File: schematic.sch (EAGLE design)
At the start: 82 parts, among them X1 SSW-108-02-S-D-RA, X2 SSW-116-02-S-TRA, X3 SSW-106-02-S-D-RA, X4 SSW-116-02-S-TRA

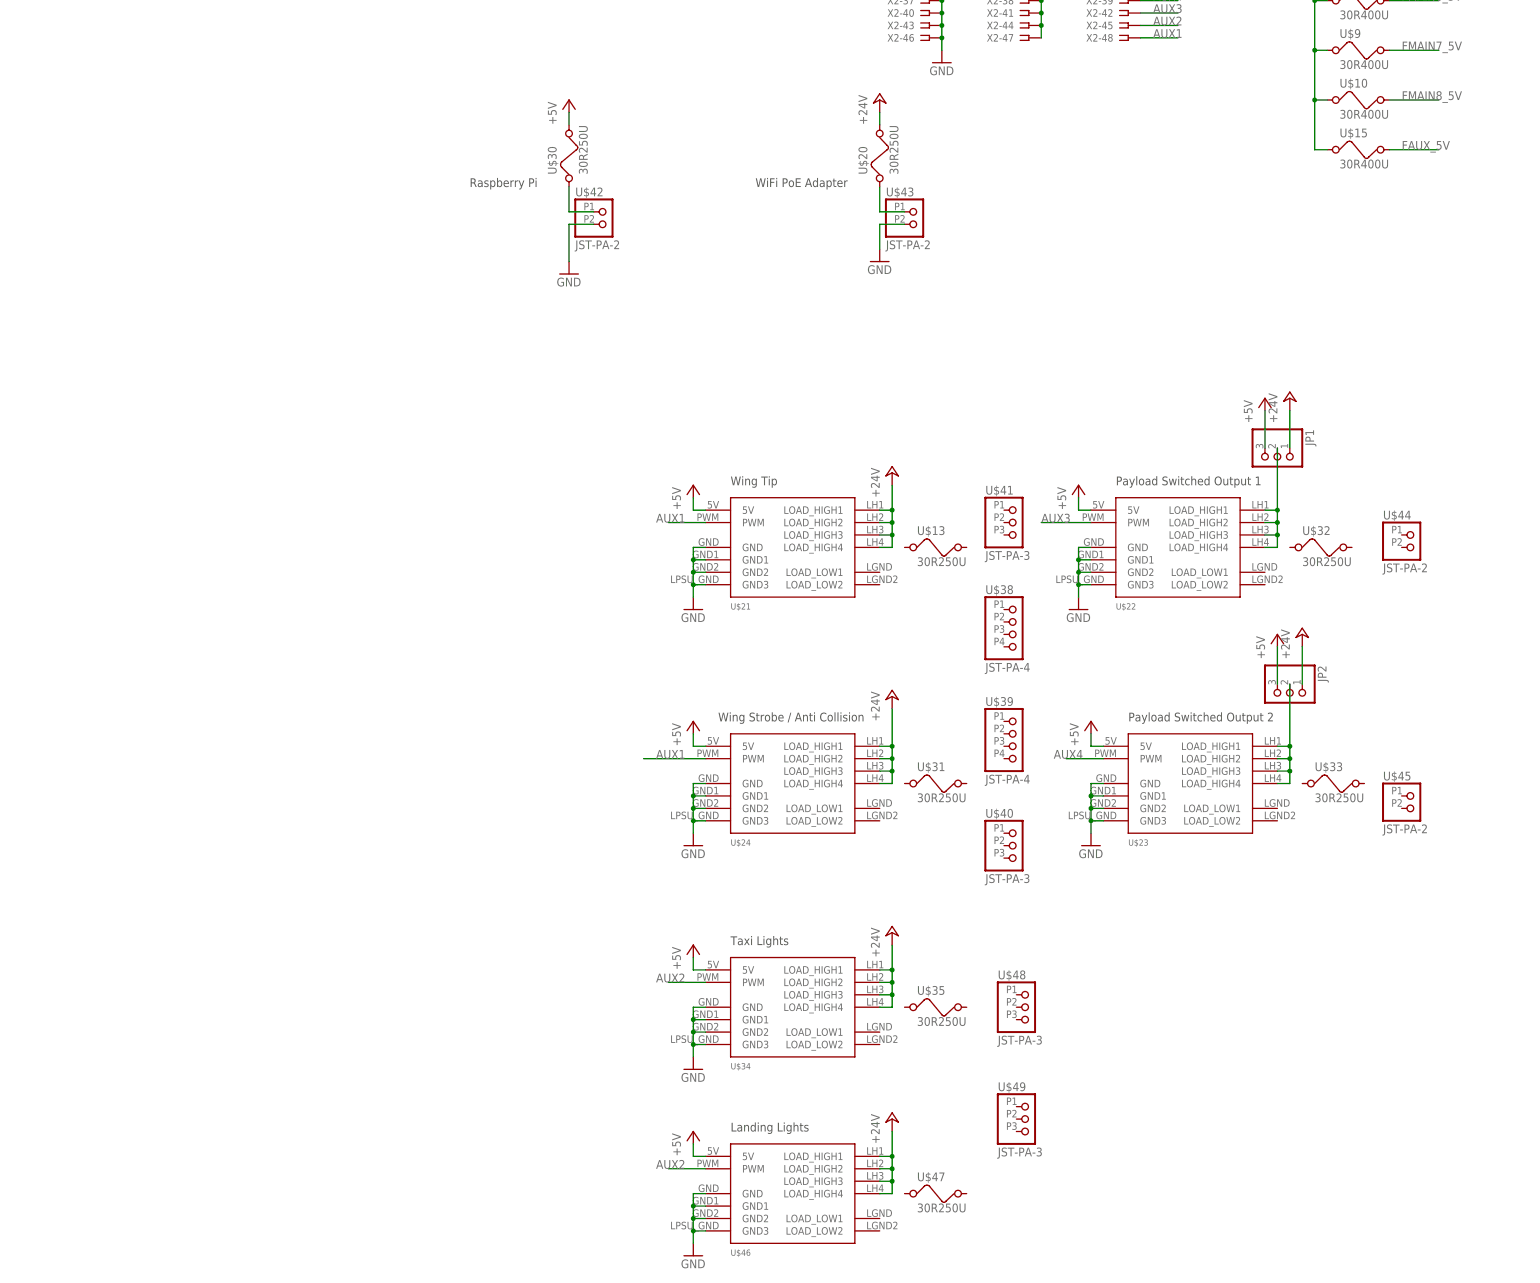
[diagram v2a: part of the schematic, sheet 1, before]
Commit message: Adding 12v rail and connecting payloads.
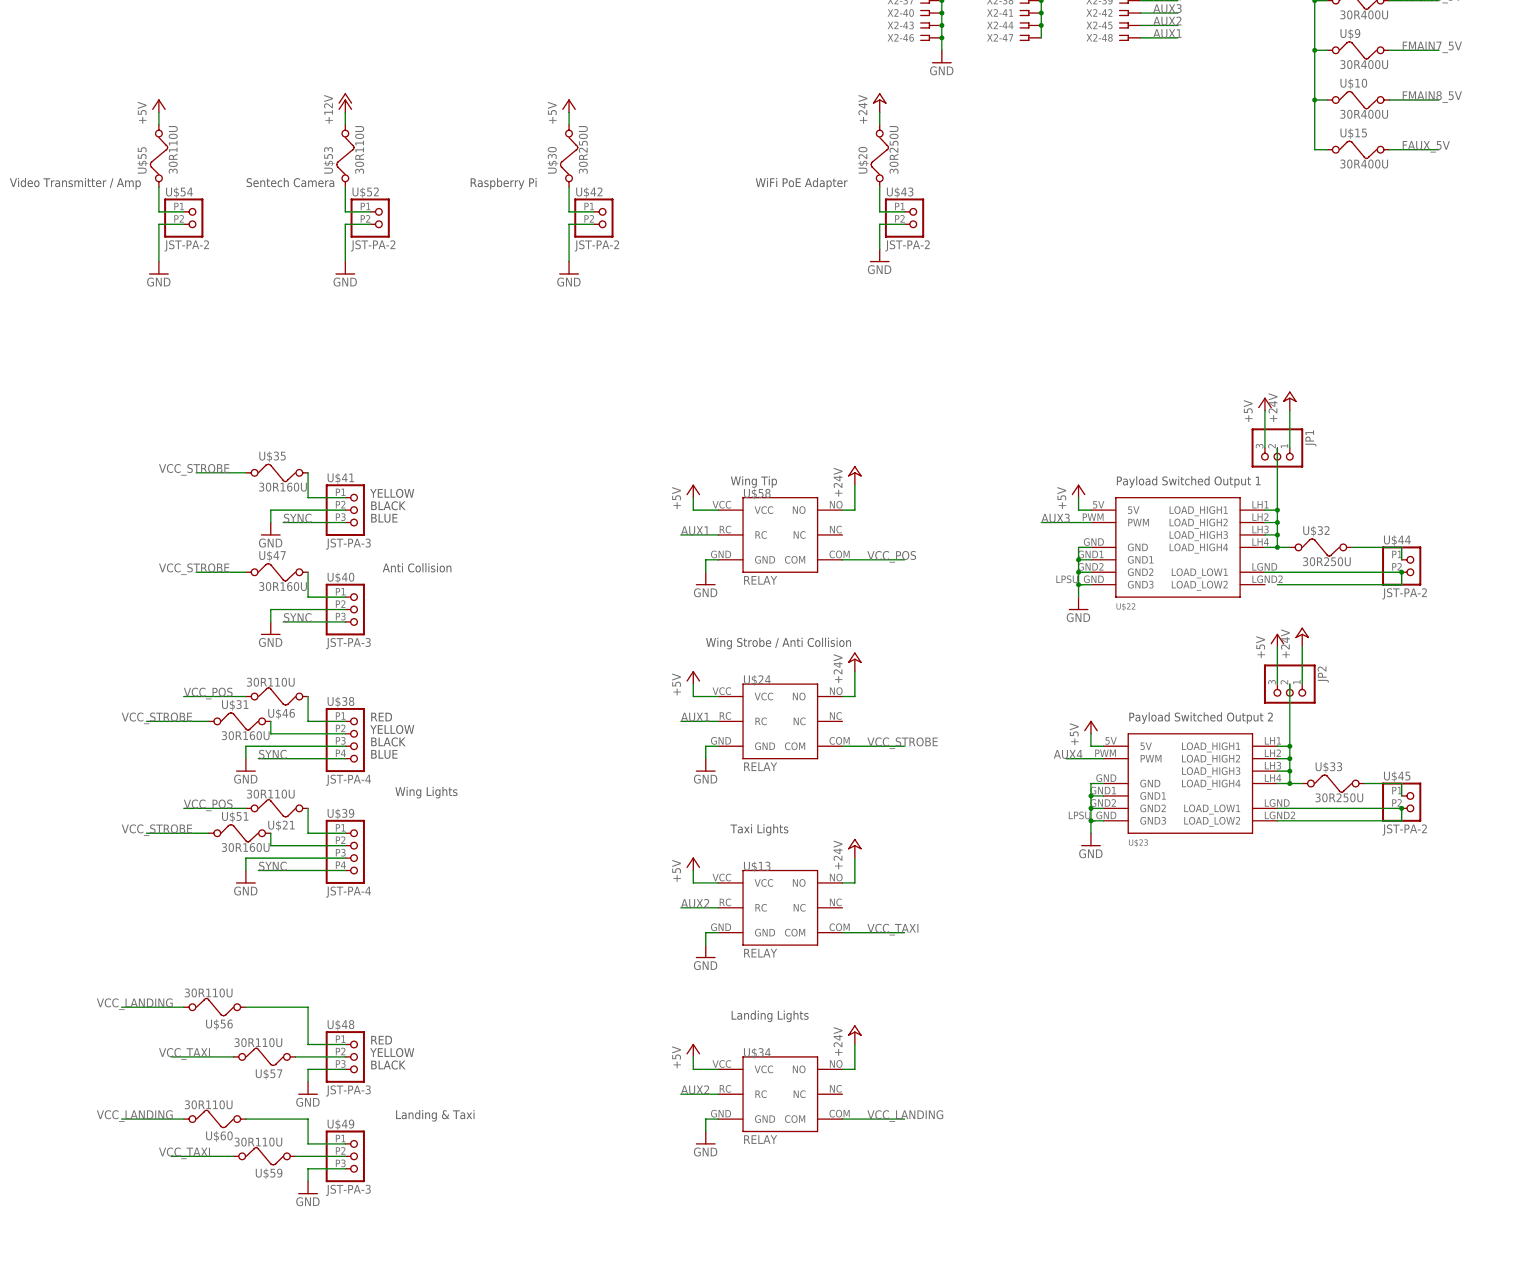
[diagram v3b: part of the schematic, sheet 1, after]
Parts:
- added C10, C9: (no value), rcl:C-USC1210
- added LED3: (no value), led:LEDCHIPLED_0805
- added R16: (no value), rcl:R-US_M0805
- added U$50: PYB10, cui:PYB10
- added U$51: 30R160U, littelfuse:30R160U
- added U$52, U$54: JST-PA-2, jst:JST-PA-2
- added U$53, U$55, U$56, U$57, U$59, U$60: 30R110U, littelfuse:30R110U
- added U$58: RELAY, pololu:RELAY
- U$13: value 30R250U -> RELAY; device littelfuse:30R250U -> pololu:RELAY
- U$2: value VHE100W -> VHB150W; device cui:VHE100W -> cui:VHB150W
- U$21, U$46: value MED_MOSFET -> 30R110U; device pololu:MED_MOSFET -> littelfuse:30R110U
- U$24, U$34: value MED_MOSFET -> RELAY; device pololu:MED_MOSFET -> pololu:RELAY
- U$31, U$35, U$47: value 30R250U -> 30R160U; device littelfuse:30R250U -> littelfuse:30R160U
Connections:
- new net +12V: LED3.A, U$50.VO+, U$53.2
- new net 12V_ONOFF: U$29.1A1, U$50.CTRL
- new net N$14: U$52.1, U$53.1
- new net N$20: U$54.1, U$55.1
- new net N$21: LED3.C, R16.2
- new net N$22: U$23.LOAD_LOW1, U$23.LOAD_LOW2, U$45.2
- new net N$23: U$33.2, U$45.1
- new net N$24: U$22.LOAD_LOW1, U$44.2
- new net N$25: U$32.2, U$44.1
- new net N$26: U$38.1, U$46.1
- new net N$27: U$31.2, U$38.2
- new net N$28: U$21.1, U$39.1
- new net N$29: U$39.2, U$51.2
- new net N$30: U$35.2, U$41.1
- new net N$31: U$40.1, U$47.2
- new net N$32: U$49.2, U$59.1
- new net N$33: U$49.1, U$60.1
- new net N$34: U$48.2, U$57.1
- new net N$35: U$48.1, U$56.1
- new net SYNC: U$38.4, U$39.4, U$40.3, U$41.3
- new net VCC_LANDING: U$34.COM, U$56.2, U$60.2
- new net VCC_POS: U$21.2, U$46.2, U$58.COM
- new net VCC_STROBE: U$24.COM, U$31.1, U$35.1, U$47.1, U$51.1
- new net VCC_TAXI: U$13.COM, U$57.2, U$59.2
- net +24V: now also U$13.NO, U$24.NO, U$34.NO, U$58.NO; no longer U$21.LOAD_HIGH1, U$21.LOAD_HIGH2, U$21.LOAD_HIGH3, U$21.LOAD_HIGH4, U$24.LOAD_HIGH1, U$24.LOAD_HIGH2, U$24.LOAD_HIGH3, U$24.LOAD_HIGH4, U$34.LOAD_HIGH1, U$34.LOAD_HIGH2, U$34.LOAD_HIGH3, U$34.LOAD_HIGH4, U$46.LOAD_HIGH1, U$46.LOAD_HIGH2, U$46.LOAD_HIGH3, U$46.LOAD_HIGH4
- net +5V: now also U$13.VCC, U$24.VCC, U$34.VCC, U$55.2, U$58.VCC; no longer U$21.5V, U$24.5V, U$34.5V, U$46.5V
- net 24V_ONOFF: no longer U$29.1A1
- net AUX1: now also U$24.RC, U$58.RC; no longer U$21.PWM, U$24.PWM
- net AUX2: now also U$13.RC, U$34.RC; no longer U$34.PWM, U$46.PWM
- net GND: now also R16.1, U$13.GND, U$38.3, U$39.3, U$40.2, U$41.2, U$48.3, U$49.3, U$50.VO-, U$52.2, U$54.2, U$58.GND; no longer U$21.GND, U$21.GND1, U$21.GND2, U$21.GND3, U$24.GND1, U$24.GND2, U$24.GND3, U$34.GND1, U$34.GND2, U$34.GND3, U$46.GND, U$46.GND1, U$46.GND2, U$46.GND3
- net N$16: now also U$33.1
- net N$4: now also U$32.1
- net V+: now also C10.1, C9.1, U$50.VIN; no longer U$28.NC, U$28.NC1, U$29.NC, U$29.NC1
- net V-: now also C10.2, C9.2, U$50.GND
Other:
- note added: "Anti Collision"
- note added: "BLACK"
- note added: "BLUE"
- note added: "Landing & Taxi"
- note added: "RED"
- note added: "Sentech Camera"
- note added: "Video Transmitter / Amp"
- note added: "Wing Lights"
- note added: "YELLOW"
- moved on the sheet: U$31, U$35, U$38, U$39, U$40, U$41, U$44, U$47, U$48, U$49

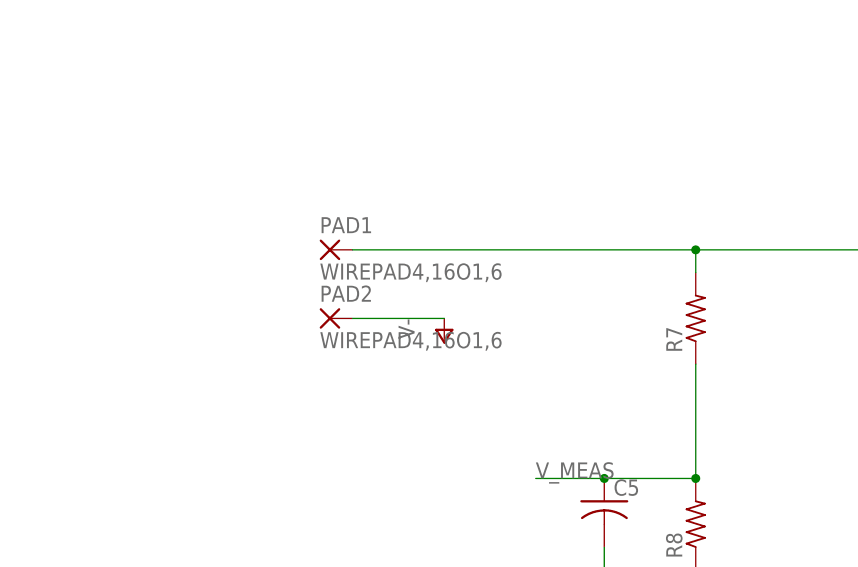
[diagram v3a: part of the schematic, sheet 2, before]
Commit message: Adding new power connector.
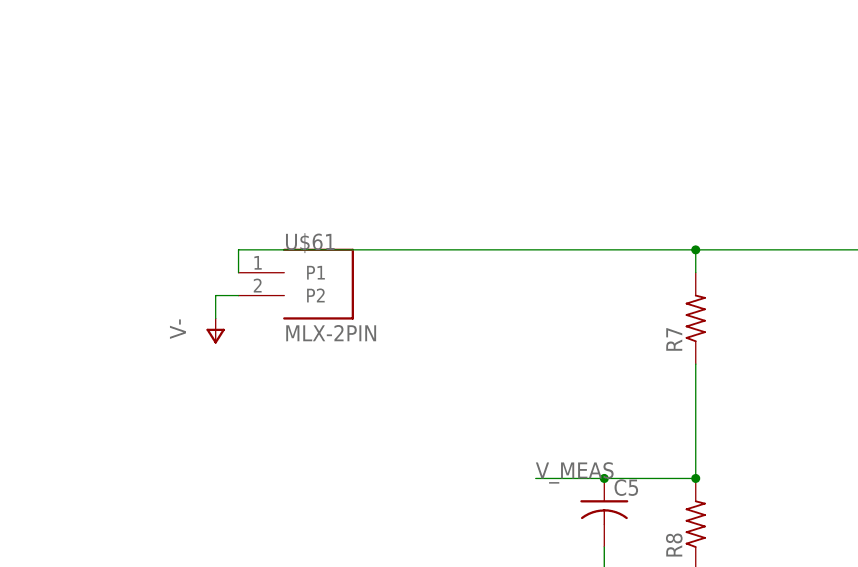
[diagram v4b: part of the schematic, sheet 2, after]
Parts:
- removed PAD1, PAD2: WIREPAD4,16O1,6, wirepad:WIREPAD4,16O1,6
- added U$61: MLX-2PIN, molex:MLX-2PIN
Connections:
- net N$12: now also U$61.P1; no longer PAD1.P
- net V-: now also U$61.P2; no longer PAD2.P
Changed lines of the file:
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@@
 <part name="X2" library="con-samtec" deviceset="SSW-116-02-S-T" device="RA"/>
 <part name="X3" library="con-samtec" deviceset="SSW-106-02-S-D" device="-RA"/>
-<part name="PAD1" library="wirepad" deviceset="WIREPAD" device="4,16O1,6"/>
-<part name="PAD2" library="wirepad" deviceset="WIREPAD" device="4,16O1,6"/>
 <part name="U$1" library="cui" deviceset="VHE100W" device=""/>
 <part name="U$3" library="littelfuse" deviceset="30R400U" device=""/>
@@
 <part name="U$21" library="littelfuse" deviceset="30R110U" device=""/>
 <part name="U$46" library="littelfuse" deviceset="30R110U" device=""/>
+<part name="U$61" library="molex" deviceset="MLX-2PIN" device=""/>
 </parts>
 <sheets>
@@
 </plain>
 <instances>
-<instance part="PAD1" gate="G$1" x="170.18" y="83.82"/>
-<instance part="PAD2" gate="G$1" x="170.18" y="76.2"/>
 <instance part="U$1" gate="G$1" x="-43.18" y="106.68"/>
-<instance part="P-1" gate="1" x="182.88" y="73.66"/>
+<instance part="P-1" gate="1" x="157.48" y="73.66"/>
 <instance part="P+2" gate="1" x="-81.28" y="33.02"/>
 <instance part="P-2" gate="1" x="-81.28" y="99.06"/>
@@
 <instance part="P+35" gate="1" x="-25.4" y="-43.18"/>
 <instance part="GND33" gate="1" x="-25.4" y="-68.58"/>
+<instance part="U$61" gate="G$1" x="165.1" y="78.74"/>
 </instances>
 <busses>
@@
 <net name="V-" class="0">
 <segment>
-<pinref part="P-1" gate="1" pin="V-"/>
-<pinref part="PAD2" gate="G$1" pin="P"/>
-<wire x1="182.88" y1="76.2" x2="172.72" y2="76.2" width="0.1524" layer="91"/>
-</segment>
-<segment>
 <pinref part="C3" gate="G$1" pin="1"/>
 <pinref part="P-2" gate="1" pin="V-"/>
@@
 <junction x="-76.2" y="-63.5"/>
 </segment>
+<segment>
+<pinref part="U$61" gate="G$1" pin="P2"/>
+<pinref part="P-1" gate="1" pin="V-"/>
+<wire x1="160.02" y1="78.74" x2="157.48" y2="78.74" width="0.1524" layer="91"/>
+<wire x1="157.48" y1="78.74" x2="157.48" y2="76.2" width="0.1524" layer="91"/>
+</segment>
 </net>
 <net name="V+" class="0">
@@
 <wire x1="236.22" y1="83.82" x2="246.38" y2="83.82" width="0.1524" layer="91"/>
 <wire x1="210.82" y1="81.28" x2="210.82" y2="83.82" width="0.1524" layer="91"/>
-<junction x="210.82" y="83.82"/>
 <pinref part="U$17" gate="G$1" pin="VIN-"/>
 <wire x1="246.38" y1="81.28" x2="246.38" y2="83.82" width="0.1524" layer="91"/>
@@
 <wire x1="236.22" y1="66.04" x2="236.22" y2="83.82" width="0.1524" layer="91"/>
 <junction x="236.22" y="83.82"/>
-<pinref part="PAD1" gate="G$1" pin="P"/>
-<wire x1="172.72" y1="83.82" x2="210.82" y2="83.82" width="0.1524" layer="91"/>
-</segment>
-</net>
+<pinref part="U$61" gate="G$1" pin="P1"/>
+<wire x1="160.02" y1="81.28" x2="160.02" y2="83.82" width="0.1524" layer="91"/>
+<wire x1="160.02" y1="83.82" x2="210.82" y2="83.82" width="0.1524" layer="91"/>
+<junction x="210.82" y="83.82"/>
+</segment>
+</net>

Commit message: Removing some components space doesn't allow for.  Established basic layout.
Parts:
- removed C10, C9: (no value), rcl:C-USC1210
- removed JP2: (no value), pinhead:PINHD-1X3
- removed LED3: (no value), led:LEDCHIPLED_0805
- removed R16: (no value), rcl:R-US_M0805
- removed U$11: 30R160U, littelfuse:30R160U
- removed U$23: MED_MOSFET, pololu:MED_MOSFET
- removed U$33: 30R250U, littelfuse:30R250U
- removed U$34: RELAY, pololu:RELAY
- removed U$45, U$52: JST-PA-2, jst:JST-PA-2
- removed U$50: PYB10, cui:PYB10
- removed U$53: 30R110U, littelfuse:30R110U
- added F30: 30R160U, littelfuse:30R160U
- added H1, H2, H3, H4: MOUNT-HOLE3.6, holes:MOUNT-HOLE3.6
- added J2: MLX-2PIN, molex:MLX-2PIN
- renumbered U$1 to U1, U$10 to F8, U$12 to F29, U$13 to U9, U$14 to J5, U$15 to F9, U$16 to F10, U$17 to U6, U$18 to J3, U$19 to F28, U$2 to U2, U$20 to F11, U$21 to F22, U$22 to U11, U$24 to U8, U$25 to U4, U$26 to U5, U$27 to J4, U$28 to SW1, U$29 to SW2, U$3 to F1, U$30 to F12, U$31 to F21, U$32 to F16, U$35 to F18, U$36 to F15, U$37 to J10, U$38 to J19, U$39 to J20, U$4 to F2, U$40 to J18, U$41 to J17, U$42 to J12, U$43 to J11, U$44 to J15, U$46 to F20, U$47 to F19, U$48 to J21, U$49 to J22, U$5 to F3, U$51 to F23, U$54 to J14, U$55 to F14, U$56 to F24, U$57 to F25, U$58 to U7, U$59 to F27, U$6 to F4, U$60 to F26, U$61 to J1, U$7 to F5, U$8 to F6, U$9 to F7, X1 to J8, X2 to J6, X3 to J9, X4 to J7
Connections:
- removed net +12V: LED3.A, U$50.VO+, U$53.2
- removed net N$14: U$52.1, U$53.1
- removed net N$16: JP2.2, U$23.LOAD_HIGH1, U$23.LOAD_HIGH2, U$23.LOAD_HIGH3, U$23.LOAD_HIGH4, U$33.1
- removed net N$21: LED3.C, R16.2
- removed net N$22: U$23.LOAD_LOW1, U$23.LOAD_LOW2, U$45.2
- removed net N$23: U$33.2, U$45.1
- removed net VCC_LANDING: F24.2, F26.2, U$34.COM
- net +24V: no longer JP2.1, U$34.NO
- net +5V: now also F30.2; no longer JP2.3, U$11.2, U$23.5V, U$34.VCC
- net 12V_ONOFF: no longer U$50.CTRL
- net AUX2: no longer U$34.RC
- net AUX4: no longer U$23.PWM
- net FRFD_5V: now also F30.1; no longer U$11.1
- net GND: no longer R16.1, U$23.GND, U$23.GND1, U$23.GND2, U$23.GND3, U$34.GND, U$50.VO-, U$52.2
- net N$12: now also J2.P1
- net V+: no longer C10.1, C9.1, U$50.VIN
- net V-: now also J2.P2; no longer C10.2, C9.2, U$50.GND
- net VCC_TAXI: now also F24.2, F26.2
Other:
- note removed: "Payload Switched Output 2"
- note removed: "Sentech Camera"

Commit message: Updating drawing with new right angle connectors on a single board side.
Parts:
- removed H1, H2, H3, H4: MOUNT-HOLE3.6, holes:MOUNT-HOLE3.6
- removed J2: MLX-2PIN, molex:MLX-2PIN
- added H5, H6, H7, H8: MOUNT-HOLE3.2, holes:MOUNT-HOLE3.2
- J1: value MLX-2PIN -> MEGAFIT-4SKT-RA; device molex:MLX-2PIN -> molex:MEGAFIT-4SKT-RA
- J10, J19, J20: value JST-PA-4 -> JST-PA-SMT-RA-4; device jst:JST-PA-4 -> jst:JST-PA-SMT-RA-4
- J11, J12, J14, J15: value JST-PA-2 -> JST-PA-SMT-RA-2; device jst:JST-PA-2 -> jst:JST-PA-SMT-RA-2
- J17, J18, J21, J22: value JST-PA-3 -> JST-PA-SMT-RA-3; device jst:JST-PA-3 -> jst:JST-PA-SMT-RA-3
- J7: value SSW-116-02-S-TRA -> SSW-108-02-S-TRA; device con-samtec:SSW-116-02-S-TRA -> con-samtec:SSW-108-02-S-TRA
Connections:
- removed net N$24: J15.2, U11.LOAD_LOW1
- new net N$16: J15.2, U11.LOAD_LOW1, U11.LOAD_LOW2
- net AUX1: no longer J7-3.1
- net AUX2: no longer J7-6.1
- net AUX3: no longer J7-9.1
- net AUX4: no longer J7-12.1
- net AUX5: no longer J7-15.1
- net AUX6: no longer J7-18.1
- net FAUX_5V: no longer J7-11.1, J7-14.1, J7-17.1, J7-2.1, J7-44.1, J7-5.1, J7-8.1
- net FMAIN1_5V: now also J7-2.1; no longer J7-20.1
- net FMAIN2_5V: now also J7-5.1; no longer J7-23.1
- net FMAIN3_5V: now also J7-8.1; no longer J7-26.1
- net FMAIN4_5V: now also J7-11.1; no longer J7-29.1
- net FMAIN5_5V: now also J7-14.1; no longer J7-32.1
- net FMAIN6_5V: now also J7-17.1; no longer J7-35.1
- net FMAIN7_5V: now also J7-20.1; no longer J7-38.1
- net FMAIN8_5V: now also J7-23.1; no longer J7-41.1
- net GND: no longer J7-25.1, J7-28.1, J7-31.1, J7-34.1, J7-37.1, J7-40.1, J7-43.1, J7-46.1
- net MAIN1: now also J7-3.1; no longer J7-21.1
- net MAIN2: now also J7-6.1; no longer J7-24.1
- net MAIN3: now also J7-9.1; no longer J7-27.1
- net MAIN4: now also J7-12.1; no longer J7-30.1
- net MAIN5: now also J7-15.1; no longer J7-33.1
- net MAIN6: now also J7-18.1; no longer J7-36.1
- net MAIN7: now also J7-21.1; no longer J7-39.1
- net MAIN8: now also J7-24.1; no longer J7-42.1
- net N$12: now also J1.P$1, J1.P$2; no longer J1.P1, J2.P1
- net SBUS: no longer J7-45.1
- net V-: now also J1.P$3, J1.P$4; no longer J1.P2, J2.P2
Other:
- moved on the sheet: J15, J7-1, J7-10, J7-11, J7-12, J7-13, J7-14, J7-15, J7-16, J7-17, J7-18, J7-19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
